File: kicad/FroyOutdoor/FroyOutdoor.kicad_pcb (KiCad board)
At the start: 2 copper layers, 77.6 x 47.2 mm, 28 parts, among them IC1 ESP-WROOM-02U__4MB_, J1 Conn_01x06, Q1 Q_NPN_BEC, Q2 Q_NPN_BEC, Q3 Q_NPN_BEC, SW1 SW_SPST, U2 BME280

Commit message: Froy Outdoor 2.1, now with transistor controlling sensor and battery measurement
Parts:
- added Q4: Q_NPN_BEC, Package_TO_SOT_SMD:SOT-23, F.Cu at (69.4, 62.9)
- R4: renamed from R11; value 12k -> 10k
- R5: renamed from R9; value 12k -> 10k
- R6: renamed from R8; value 12k -> 10k
- moved R1 11.3 mm to (66.1, 68.7)
- moved R2 11.3 mm to (63.6, 68.7)
- moved R9 6.35 mm to (71.3, 68.7)
- moved C3 6.29 mm to (74.0, 68.7)
- moved R8 5.88 mm to (68.7, 68.7)
- moved R11 1.58 mm to (72.8, 62.9)
- renumbered R5 to R10, R4 to R11, R6 to R2, R2 to R7, R7 to R8, R10 to R9
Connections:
- C2 pad 2: +3V3 -> +3.3VP
- IC1 pad 4: (no net) -> /PWR_ENABLE
- R1 pad 1: +3V3 -> +3.3VP
- R2 pad 1: +3V3 -> +3.3VP
- R8 pad 1: +3V3 -> +3.3VP
- U2 pad 2: +3V3 -> +3.3VP
- U2 pad 6: +3V3 -> +3.3VP
- U2 pad 8: +3V3 -> +3.3VP
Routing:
- net +3.3VP: track 0.00 -> 55.9 mm, vias 0 -> 4
- net +3V3: track 114.5 -> 68.6 mm, vias 4 -> 2
- net /I2C_CLK: track 42.4 -> 48.1 mm
- net /I2C_SDA: track 46.6 -> 51.4 mm
- net /BATT_SENS: track 39.0 -> 43.1 mm, vias 0 -> 2
- net /PWR_ENABLE: track 0.00 -> 3.54 mm
- net Net-(IC1-Pad6): track 3.48 -> 4.07 mm
- net GNDREF: vias 4 -> 5
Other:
- board text added: "0.1uF NPN"
- board text added: "2021-09-12"
- board text added: "4k7 4k7 10k 10k 10k 10k 10k 47k (!) 22k (!) 2k2 10k"
- board text added: "C1-C3 Q1-Q4"
- board text added: "v2.1"
- board text removed: "0.1uF 0.1uF 0.1uF"
- board text removed: "2021-06-25"
- board text removed: "4k7 10k 10k 10k 270 4k7 47k 12k 12k 22k 12k"
- board text removed: "C1 C2 C3"
- board text removed: "v2.0"

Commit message: FroyOutdoor v2.2 - removed power transistor again, used Omron button
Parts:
- removed Q4: Q_NPN_BEC, Package_TO_SOT_SMD:SOT-23
- D1: footprint LED_SMD:LED_1206_3216Metric_Pad1.42x1.75mm_HandSolder -> LED_SMD:LED_0805_2012Metric
- R1, R2: value 4k7 -> 10k
- R8: value 47k -> 4M7
- R9: value 22k -> 2M2
- SW1: value SW_SPST -> SW_MEC_5E; footprint Button_Switch_SMD:SW_SPST_CK_RS282G05A3 -> xrstf:SW_SPST_Omron_B3FS-100xP
- moved R1 8.47 mm to (72.2, 62.8)
- moved R2 8.25 mm to (69.3, 62.8)
- moved SW1 2.59 mm to (65.7, 31.6), turned to 180 degrees
- moved C2 2.45 mm to (48.8, 48.0)
- moved R11 2.28 mm to (75.1, 62.8)
- moved C3 1.12 mm to (75.0, 68.4)
- moved R9 0.93 mm to (72.2, 68.4)
- moved R8 0.72 mm to (69.3, 68.4), turned to 270 degrees
- moved R7 0.35 mm to (66.5, 62.8)
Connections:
- C2 pad 2: +3.3VP -> +3V3
- IC1 pad 4: /PWR_ENABLE -> (no net)
- R1 pad 1: +3.3VP -> +3V3
- R2 pad 1: +3.3VP -> +3V3
- R8 pad 1: +3.3VP -> +3V3
- SW1 pad 2: GNDREF -> (no net)
- U2 pad 2: +3.3VP -> +3V3
- U2 pad 6: +3.3VP -> +3V3
- U2 pad 8: +3.3VP -> +3V3
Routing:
- net +3.3VP: track 55.9 -> 0.00 mm, vias 4 -> 0
- net +3V3: track 68.6 -> 112.6 mm
- net Net-(IC1-Pad6): track 4.07 -> 9.48 mm, vias 0 -> 2
- net /I2C_SDA: track 51.4 -> 46.8 mm
- net /PWR_ENABLE: track 3.54 -> 0.00 mm
- net /I2C_CLK: track 48.1 -> 44.7 mm
- net /WAKE_UP: track 39.4 -> 41.4 mm
- net /BATT_SENS: track 43.1 -> 44.7 mm
- net /RST: track 43.8 -> 45.4 mm
- net GNDREF: track 45.1 -> 45.7 mm
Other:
- board text added: "10K 10K 10K 10K 10K 10K 10K 4.7M 2.2M 1-2.2K 10K"
- board text added: "2021-09-24"
- board text added: "C1-C3 Q1-Q3"
- board text added: "ESP-WROOM-02U/D Omron B3FS-10xx Keystone 1051 BME280/680, BMP180"
- board text added: "Microcontroller Button Battery Holder Sensor"
- board text added: "v2.2"
- board text removed: "2021-09-12"
- board text removed: "4k7 4k7 10k 10k 10k 10k 10k 47k (!) 22k (!) 2k2 10k"
- board text removed: "Arduino IDE settings: -> Generic ESP8266 Board -> Reset mode: dtr (aka nodemcu) -> Flash Size: 2MB (FS: 64KB) -> Flash Frequency: 26MHz"
- board text removed: "C1-C3 Q1-Q4"
- board text removed: "v2.1"

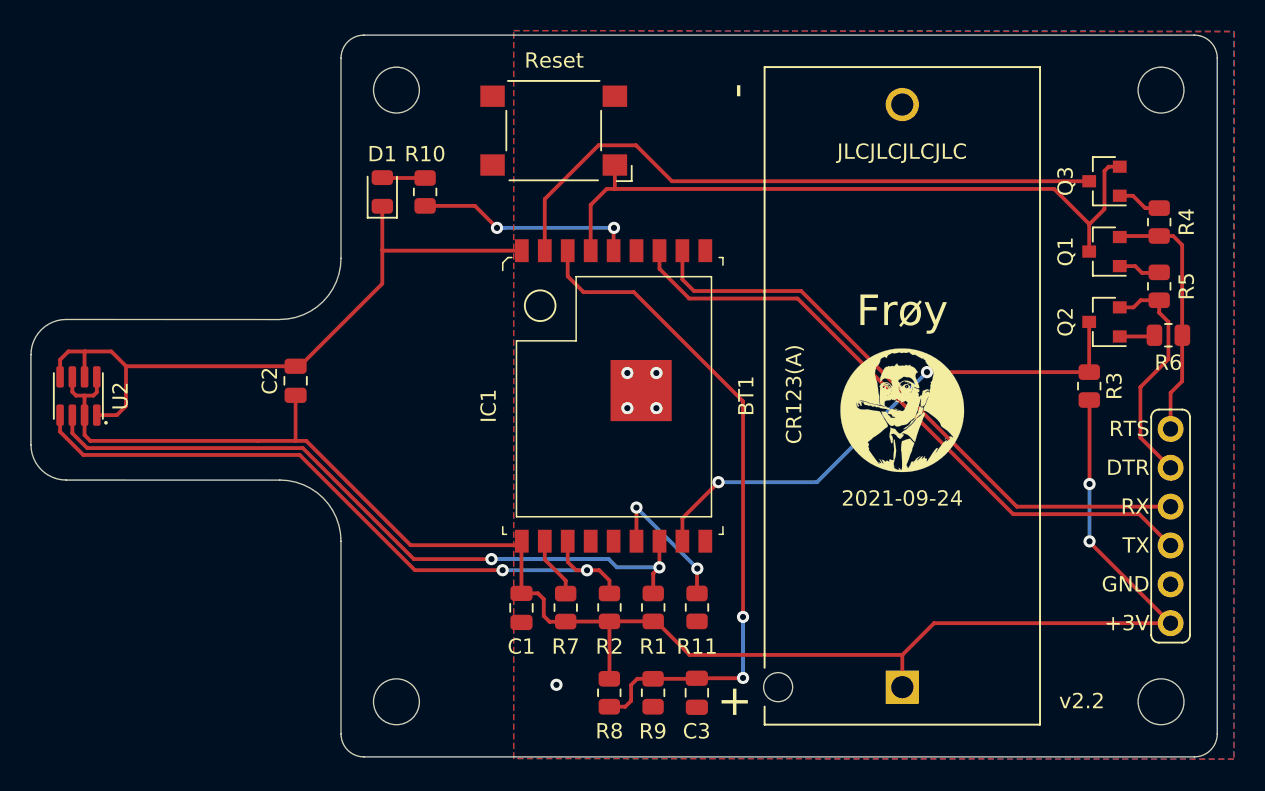
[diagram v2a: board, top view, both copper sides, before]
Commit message: FroyOutdoor v2.3 - expose I2C SDA/SCL pins to make it easy to reuse the board for quick experiments with other breakout boards
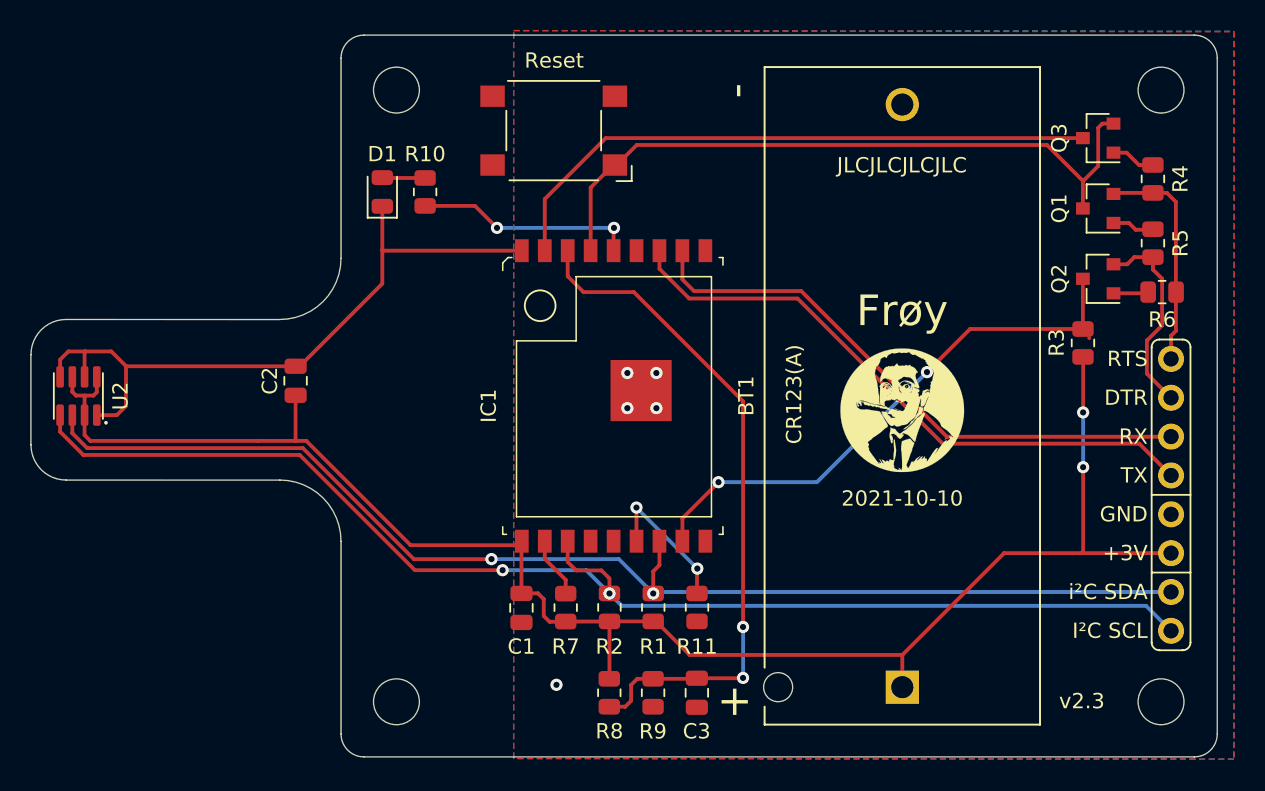
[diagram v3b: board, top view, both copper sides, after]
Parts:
- J1: value Conn_01x06 -> Conn_01x08; footprint xrstf:PinHeader_1x06_P2.54mm_Vertical -> xrstf:PinHeader_1x08_P2.54mm_Vertical
- moved Q1 2.85 mm to (101.3, 36.7)
- moved Q3 2.85 mm to (101.3, 32.1)
- moved R3 2.85 mm to (100.3, 45.5)
- moved R4 2.85 mm to (104.9, 34.8)
- moved R5 2.85 mm to (104.9, 39.0)
- moved R6 2.85 mm to (105.5, 42.2)
- moved Q2 2.85 mm to (101.3, 41.3)
- moved J1 0.50 mm to (106.1, 64.4)
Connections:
- J1 pad 1: +3V3 -> /I2C_CLK
- J1 pad 2: GNDREF -> /I2C_SDA
- J1 pad 3: /TXD -> +3V3
- J1 pad 4: /RXD -> GNDREF
- J1 pad 5: /DTR -> /TXD
- J1 pad 6: /RTS -> /RXD
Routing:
- net /I2C_CLK: track 44.7 -> 84.8 mm
- net /I2C_SDA: track 46.8 -> 81.0 mm
- net /DTR: track 15.5 -> 13.2 mm
- net /RTS: track 16.7 -> 14.8 mm
- net /TXD: track 42.1 -> 40.2 mm
- net /RXD: track 40.0 -> 38.1 mm
- net +3V3: track 112.6 -> 110.8 mm
- net /WAKE_UP: track 41.4 -> 40.2 mm
- net /IO0: track 35.3 -> 36.1 mm
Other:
- board text added: "2021-10-10"
- board text added: "I²C SCL"
- board text added: "I²C SCL (GPIO 14)"
- board text added: "i²C SDA"
- board text added: "i²C SDA (GPIO 2)"
- board text added: "v2.3"
- board text added: "μ ctrl button btr. holder sensor"
- board text removed: "2021-09-24"
- board text removed: "Microcontroller Button Battery Holder Sensor"
- board text removed: "v2.2"
